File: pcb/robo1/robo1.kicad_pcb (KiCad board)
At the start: 2 copper layers, 9 parts, among them J1 Conn_02x05_Odd_Even, J2 Conn_02x05_Odd_Even, J3 Conn_01x05_Pin, J4 Conn_01x05_Pin, U1 Pico

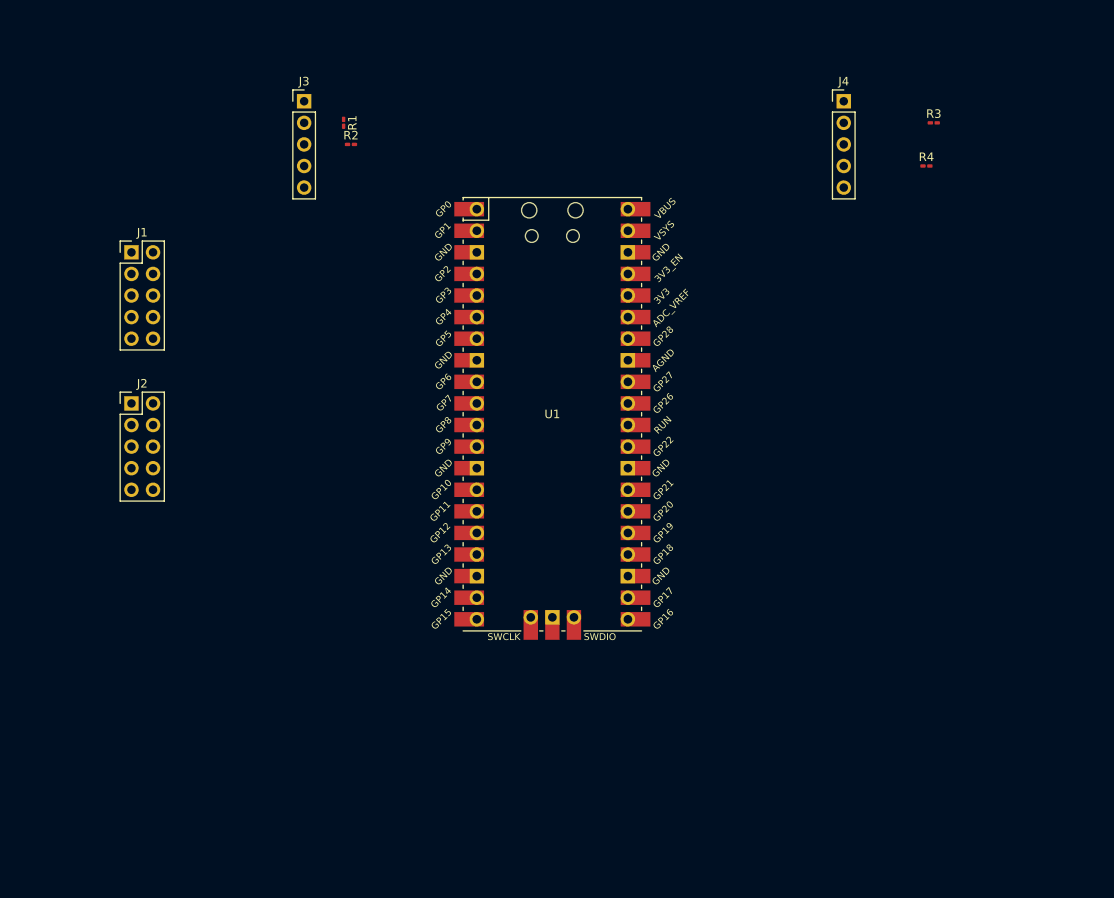
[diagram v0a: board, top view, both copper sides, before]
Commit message: pcb  outline
added mounting holes and text labels
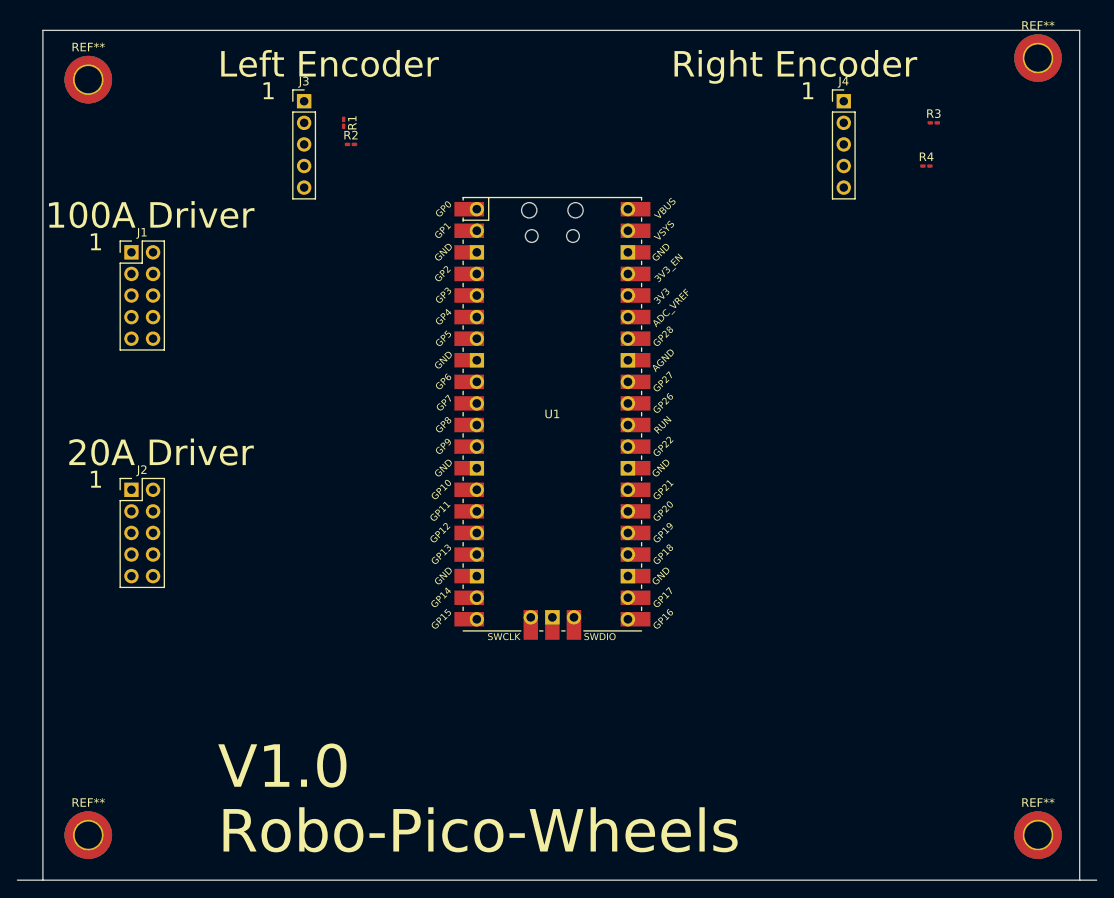
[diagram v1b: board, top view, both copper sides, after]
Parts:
- added REF**: MountingHole_3.2mm_M3_DIN965_Pad_TopBottom, MountingHole:MountingHole_3.2mm_M3_DIN965_Pad_TopBottom, F.Cu at (165.1, 48.3)
- added REF**: MountingHole_3.2mm_M3_DIN965_Pad_TopBottom, MountingHole:MountingHole_3.2mm_M3_DIN965_Pad_TopBottom, F.Cu at (53.3, 50.8)
- added REF**: MountingHole_3.2mm_M3_DIN965_Pad_TopBottom, MountingHole:MountingHole_3.2mm_M3_DIN965_Pad_TopBottom, F.Cu at (165.1, 139.7)
- added REF**: MountingHole_3.2mm_M3_DIN965_Pad_TopBottom, MountingHole:MountingHole_3.2mm_M3_DIN965_Pad_TopBottom, F.Cu at (53.3, 139.7)
- moved J2 10.2 mm to (58.4, 99.1)
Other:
- board outline added: 127 x 100 mm
- board text added: "1"
- board text added: "100A Driver"
- board text added: "20A Driver"
- board text added: "Left Encoder"
- board text added: "Right Encoder"
- board text added: "Robo-Pico-Wheels"
- board text added: "V1.0"
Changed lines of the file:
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@@
   )
   (setup
+    (stackup
+      (layer "F.SilkS" (type "Top Silk Screen"))
+      (layer "F.Paste" (type "Top Solder Paste"))
+      (layer "F.Mask" (type "Top Solder Mask") (thickness 0.01))
+      (layer "F.Cu" (type "copper") (thickness 0.035))
+      (layer "dielectric 1" (type "core") (thickness 1.51) (material "FR4") (epsilon_r 4.5) (loss_tangent 0.02))
+      (layer "B.Cu" (type "copper") (thickness 0.035))
+      (layer "B.Mask" (type "Bottom Solder Mask") (thickness 0.01))
+      (layer "B.Paste" (type "Bottom Solder Paste"))
+      (layer "B.SilkS" (type "Bottom Silk Screen"))
+      (copper_finish "ENIG")
+      (dielectric_constraints no)
+    )
     (pad_to_mask_clearance 0)
     (pcbplotparams
@@
   (net 39 "unconnected-(U1-SWCLK-Pad41)")
   (net 40 "unconnected-(U1-SWDIO-Pad43)")
+  (footprint "MountingHole:MountingHole_3.2mm_M3_DIN965_Pad_TopBottom" (layer "F.Cu")
+    (at 165.1 48.26)
+    (descr "Mounting Hole 3.2mm, M3, DIN965")
+    (tags "mounting hole 3.2mm m3 din965")
+    (attr exclude_from_pos_files exclude_from_bom)
+    (fp_text reference "REF**" (at 0 -3.8) (layer "F.SilkS")
+        (effects (font (size 1 1) (thickness 0.15)))
+    )
+    (fp_text value "MountingHole_3.2mm_M3_DIN965_Pad_TopBottom" (at 0 3.8) (layer "F.Fab")
+        (effects (font (size 1 1) (thickness 0.15)))
+    )
+    (fp_text user "${REFERENCE}" (at 0 0) (layer "F.Fab")
+        (effects (font (size 1 1) (thickness 0.15)))
+    )
+    (fp_circle (center 0 0) (end 2.8 0)
+      (stroke (width 0.15) (type solid)) (fill none) (layer "Cmts.User"))
+    (fp_circle (center 0 0) (end 3.05 0)
+      (stroke (width 0.05) (type solid)) (fill none) (layer "F.CrtYd"))
+    (pad "1" thru_hole circle (at 0 0) (size 3.6 3.6) (drill 3.2) (layers "*.Cu" "*.Mask"))
+    (pad "1" connect circle (at 0 0) (size 5.6 5.6) (layers "F.Cu" "F.Mask"))
+    (pad "1" connect circle (at 0 0) (size 5.6 5.6) (layers "B.Cu" "B.Mask"))
+  )
   (footprint "Resistor_SMD:R_0201_0603Metric_Pad0.64x0.40mm_HandSolder" (layer "F.Cu")
     (at 83.3875 55.88 -90)
@@
     )
   )
+  (footprint "MountingHole:MountingHole_3.2mm_M3_DIN965_Pad_TopBottom" (layer "F.Cu")
+    (at 53.34 50.8)
+    (descr "Mounting Hole 3.2mm, M3, DIN965")
+    (tags "mounting hole 3.2mm m3 din965")
+    (attr exclude_from_pos_files exclude_from_bom)
+    (fp_text reference "REF**" (at 0 -3.8) (layer "F.SilkS")
+        (effects (font (size 1 1) (thickness 0.15)))
+    )
+    (fp_text value "MountingHole_3.2mm_M3_DIN965_Pad_TopBottom" (at 0 3.8) (layer "F.Fab")
+        (effects (font (size 1 1) (thickness 0.15)))
+    )
+    (fp_text user "${REFERENCE}" (at 0 0) (layer "F.Fab")
+        (effects (font (size 1 1) (thickness 0.15)))
+    )
+    (fp_circle (center 0 0) (end 2.8 0)
+      (stroke (width 0.15) (type solid)) (fill none) (layer "Cmts.User"))
+    (fp_circle (center 0 0) (end 3.05 0)
+      (stroke (width 0.05) (type solid)) (fill none) (layer "F.CrtYd"))
+    (pad "1" thru_hole circle (at 0 0) (size 3.6 3.6) (drill 3.2) (layers "*.Cu" "*.Mask"))
+    (pad "1" connect circle (at 0 0) (size 5.6 5.6) (layers "F.Cu" "F.Mask"))
+    (pad "1" connect circle (at 0 0) (size 5.6 5.6) (layers "B.Cu" "B.Mask"))
+  )
   (footprint "Connector_PinHeader_2.54mm:PinHeader_2x05_P2.54mm_Vertical" (layer "F.Cu")
-    (at 58.42 88.9)
+    (at 58.42 99.06)
     (descr "Through hole straight pin header, 2x05, 2.54mm pitch, double rows")
     (tags "Through hole pin header THT 2x05 2.54mm double row")
@@
     )
   )
+  (footprint "MountingHole:MountingHole_3.2mm_M3_DIN965_Pad_TopBottom" (layer "F.Cu")
+    (at 165.1 139.7)
+    (descr "Mounting Hole 3.2mm, M3, DIN965")
+    (tags "mounting hole 3.2mm m3 din965")
+    (attr exclude_from_pos_files exclude_from_bom)
+    (fp_text reference "REF**" (at 0 -3.8) (layer "F.SilkS")
+        (effects (font (size 1 1) (thickness 0.15)))
+    )
+    (fp_text value "MountingHole_3.2mm_M3_DIN965_Pad_TopBottom" (at 0 3.8) (layer "F.Fab")
+        (effects (font (size 1 1) (thickness 0.15)))
+    )
+    (fp_text user "${REFERENCE}" (at 0 0) (layer "F.Fab")
+        (effects (font (size 1 1) (thickness 0.15)))
+    )
+    (fp_circle (center 0 0) (end 2.8 0)
+      (stroke (width 0.15) (type solid)) (fill none) (layer "Cmts.User"))
+    (fp_circle (center 0 0) (end 3.05 0)
+      (stroke (width 0.05) (type solid)) (fill none) (layer "F.CrtYd"))
+    (pad "1" thru_hole circle (at 0 0) (size 3.6 3.6) (drill 3.2) (layers "*.Cu" "*.Mask"))
+    (pad "1" connect circle (at 0 0) (size 5.6 5.6) (layers "F.Cu" "F.Mask"))
+    (pad "1" connect circle (at 0 0) (size 5.6 5.6) (layers "B.Cu" "B.Mask"))
+  )
   (footprint "Resistor_SMD:R_0201_0603Metric_Pad0.64x0.40mm_HandSolder" (layer "F.Cu")
     (at 84.2525 58.42)
@@
       (rotate (xyz 0 0 0))
     )
+  )
+  (footprint "MountingHole:MountingHole_3.2mm_M3_DIN965_Pad_TopBottom" (layer "F.Cu")
+    (at 53.34 139.7)
+    (descr "Mounting Hole 3.2mm, M3, DIN965")
+    (tags "mounting hole 3.2mm m3 din965")
+    (attr exclude_from_pos_files exclude_from_bom)
+    (fp_text reference "REF**" (at 0 -3.8) (layer "F.SilkS")
+        (effects (font (size 1 1) (thickness 0.15)))
+    )
+    (fp_text value "MountingHole_3.2mm_M3_DIN965_Pad_TopBottom" (at 0 3.8) (layer "F.Fab")
+        (effects (font (size 1 1) (thickness 0.15)))
+    )
+    (fp_text user "${REFERENCE}" (at 0 0) (layer "F.Fab")
+        (effects (font (size 1 1) (thickness 0.15)))
+    )
+    (fp_circle (center 0 0) (end 2.8 0)
+      (stroke (width 0.15) (type solid)) (fill none) (layer "Cmts.User"))
+    (fp_circle (center 0 0) (end 3.05 0)
+      (stroke (width 0.05) (type solid)) (fill none) (layer "F.CrtYd"))
+    (pad "1" thru_hole circle (at 0 0) (size 3.6 3.6) (drill 3.2) (layers "*.Cu" "*.Mask"))
+    (pad "1" connect circle (at 0 0) (size 5.6 5.6) (layers "F.Cu" "F.Mask"))
+    (pad "1" connect circle (at 0 0) (size 5.6 5.6) (layers "B.Cu" "B.Mask"))
   )
   (footprint "Resistor_SMD:R_0201_0603Metric_Pad0.64x0.40mm_HandSolder" (layer "F.Cu")
@@
     )
   )
+  (gr_line (start 172 145) (end 45 145)
+    (stroke (width 0.1) (type default)) (layer "Edge.Cuts"))
+  (gr_line (start 170 45) (end 170 145)
+    (stroke (width 0.1) (type default)) (layer "Edge.Cuts"))
+  (gr_line (start 48 145) (end 48 45)
+    (stroke (width 0.1) (type default)) (layer "Edge.Cuts"))
+  (gr_line (start 48 45) (end 170 45)
+    (stroke (width 0.1) (type default)) (layer "Edge.Cuts"))
+  (gr_text "V1.0" (at 68.58 134.62) (layer "F.SilkS")
+    (effects (font (size 5 5) (thickness 0.2)) (justify left bottom))
+  )
+  (gr_text "Robo-Pico-Wheels" (at 68.58 142.24) (layer "F.SilkS")
+    (effects (font (size 5 5) (thickness 0.2)) (justify left bottom))
+  )
+  (gr_text "100A Driver" (at 48.26 68.58) (layer "F.SilkS")
+    (effects (font (size 3 3) (thickness 0.2)) (justify left bottom))
+  )
+  (gr_text "1" (at 73.66 53.34) (layer "F.SilkS")
+    (effects (font (size 2 2) (thickness 0.15)) (justify left bottom))
+  )
+  (gr_text "1" (at 53.34 99.06) (layer "F.SilkS")
+    (effects (font (size 2 2) (thickness 0.15)) (justify left bottom))
+  )
+  (gr_text "1" (at 53.34 71.12) (layer "F.SilkS")
+    (effects (font (size 2 2) (thickness 0.15)) (justify left bottom))
+  )
+  (gr_text "Left Encoder" (at 68.58 50.8) (layer "F.SilkS")
+    (effects (font (size 3 3) (thickness 0.2)) (justify left bottom))
+  )
+  (gr_text "20A Driver" (at 50.8 96.52) (layer "F.SilkS")
+    (effects (font (size 3 3) (thickness 0.2)) (justify left bottom))
+  )
+  (gr_text "Right Encoder" (at 121.92 50.8) (layer "F.SilkS")
+    (effects (font (size 3 3) (thickness 0.2)) (justify left bottom))
+  )
+  (gr_text "1" (at 137.16 53.34) (layer "F.SilkS")
+    (effects (font (size 2 2) (thickness 0.15)) (justify left bottom))
+  )
 )

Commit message: Add OLED to PCB
OLED added to pcb
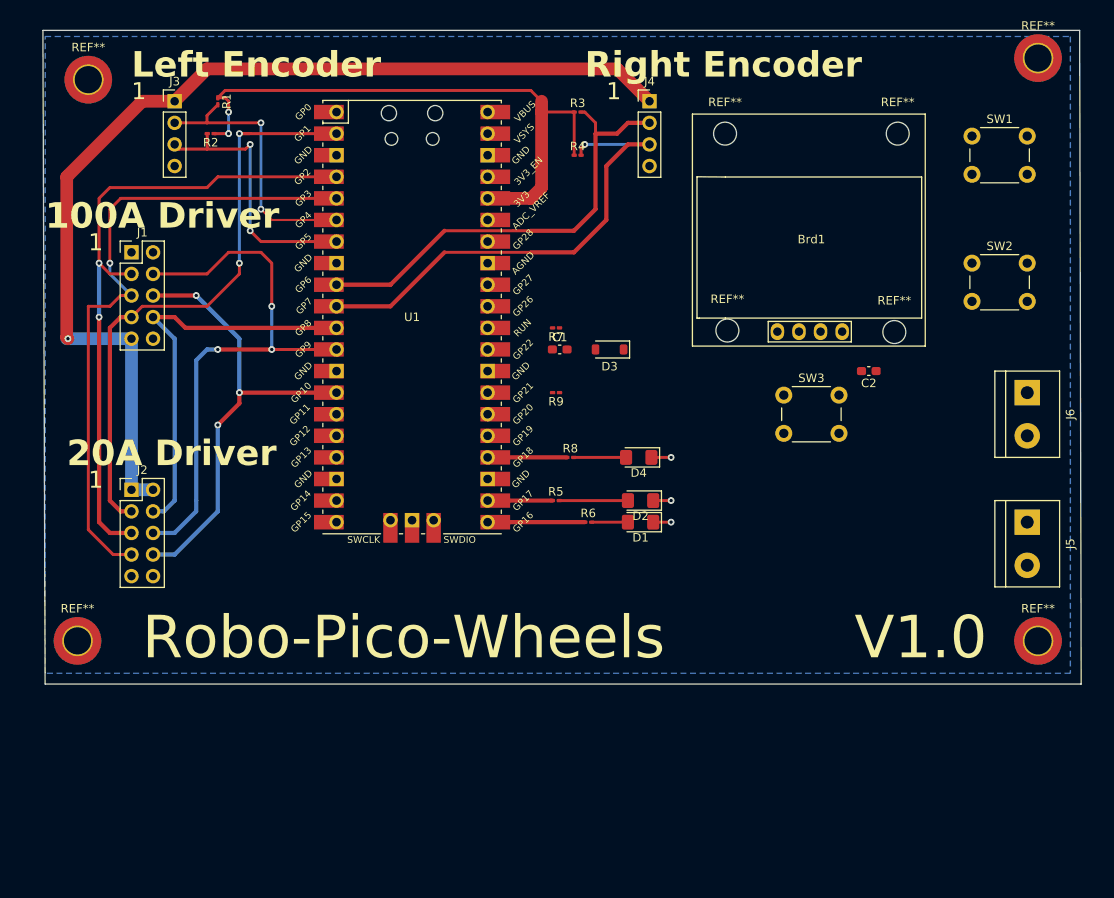
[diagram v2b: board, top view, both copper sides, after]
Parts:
- added Brd1: SSD1306, SSD1306:128x64OLED, F.Cu at (138.4, 69.8)
- added C1: .01, Capacitor_SMD:C_0603_1608Metric_Pad1.08x0.95mm_HandSolder, F.Cu at (108.8, 82.5)
- added C2: .01, Capacitor_SMD:C_0603_1608Metric_Pad1.08x0.95mm_HandSolder, F.Cu at (145.2, 85.1)
- added D1: LED, LED_SMD:LED_1206_3216Metric_Pad1.42x1.75mm_HandSolder, F.Cu at (118.3, 102.9)
- added D2: LED, LED_SMD:LED_1206_3216Metric_Pad1.42x1.75mm_HandSolder, F.Cu at (118.3, 100.3)
- added D3: 1N4148W, Diode_SMD:D_SOD-123, F.Cu at (114.7, 82.5)
- added D4: LED, LED_SMD:LED_1206_3216Metric_Pad1.42x1.75mm_HandSolder, F.Cu at (118.1, 95.2)
- added J5: Screw_Terminal_01x02, TerminalBlock:TerminalBlock_bornier-2_P5.08mm, F.Cu at (163.8, 102.9)
- added J6: Screw_Terminal_01x02, TerminalBlock:TerminalBlock_bornier-2_P5.08mm, F.Cu at (163.8, 87.6)
- added R5: 220, Resistor_SMD:R_0201_0603Metric_Pad0.64x0.40mm_HandSolder, F.Cu at (108.4, 100.3)
- added R6: 220, Resistor_SMD:R_0201_0603Metric_Pad0.64x0.40mm_HandSolder, F.Cu at (112.2, 102.9)
- added R7: 4.7K, Resistor_SMD:R_0201_0603Metric_Pad0.64x0.40mm_HandSolder, F.Cu at (108.4, 80.0)
- added R8: 220, Resistor_SMD:R_0201_0603Metric_Pad0.64x0.40mm_HandSolder, F.Cu at (110.1, 95.2)
- added R9: 4.7K, Resistor_SMD:R_0201_0603Metric_Pad0.64x0.40mm_HandSolder, F.Cu at (108.4, 87.6)
- added REF**: MountingHole_2.7mm_M2.5, MountingHole:MountingHole_2.7mm_M2.5, F.Cu at (148.6, 57.1)
- added REF**: MountingHole_2.7mm_M2.5, MountingHole:MountingHole_2.7mm_M2.5, F.Cu at (148.2, 80.5)
- added REF**: MountingHole_2.7mm_M2.5, MountingHole:MountingHole_2.7mm_M2.5, F.Cu at (128.3, 57.1)
- added REF**: MountingHole_2.7mm_M2.5, MountingHole:MountingHole_2.7mm_M2.5, F.Cu at (128.5, 80.3)
- added SW1: SW_Push, Button_Switch_THT:SW_PUSH_6mm, F.Cu at (157.3, 57.4)
- added SW2: SW_Push, Button_Switch_THT:SW_PUSH_6mm, F.Cu at (157.3, 72.4)
- added SW3: SW_Push, Button_Switch_THT:SW_PUSH_6mm, F.Cu at (135.2, 87.9)
- J3, J4: value Conn_01x05_Pin -> Conn_01x04_Pin; footprint Connector_PinHeader_2.54mm:PinHeader_1x05_P2.54mm_Vertical -> Connector_PinHeader_2.54mm:PinHeader_1x04_P2.54mm_Vertical
- moved R3 41.9 mm to (110.9, 54.6)
- moved R4 41.1 mm to (110.9, 59.7)
- moved REF** 22.9 mm to (52.1, 116.8)
- moved J4 22.9 mm to (119.4, 53.3)
- moved REF** 22.9 mm to (165.1, 116.8)
- moved U1 20.1 mm to (91.4, 78.7)
- moved R2 16.6 mm to (67.7, 57.1), turned to 180 degrees
- moved J3 15.2 mm to (63.5, 53.3)
- moved R1 15.0 mm to (68.6, 53.3)
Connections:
- U1 pad 15: unconnected-(U1-GPIO11-Pad15) -> /PWM_LEFT
- U1 pad 2: /PWM_LEFT -> unconnected-(U1-GPIO1-Pad2)
- U1 pad 21: unconnected-(U1-GPIO16-Pad21) -> Net-(U1-GPIO16)
- U1 pad 22: unconnected-(U1-GPIO17-Pad22) -> Net-(U1-GPIO17)
- U1 pad 24: unconnected-(U1-GPIO18-Pad24) -> Net-(U1-GPIO18)
- U1 pad 25: unconnected-(U1-GPIO19-Pad25) -> /I2C1_SCL
- U1 pad 26: unconnected-(U1-GPIO20-Pad26) -> /I2C1_SDA
- U1 pad 29: unconnected-(U1-GPIO22-Pad29) -> Net-(D3-A)
- U1 pad 36: unconnected-(U1-3V3-Pad36) -> +3.3V
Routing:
- net +5V: track 0.00 -> 122.5 mm, vias 0 -> 1
- net /LEFTDIRB: track 0.00 -> 76.6 mm, vias 0 -> 1
- net /LEFTDIRA: track 0.00 -> 75.8 mm, vias 0 -> 2
- net +3.3V: track 0.00 -> 71.9 mm, vias 0 -> 2
- net /PWM_LEFT: track 0.00 -> 70.5 mm, vias 0 -> 2
- net /RIGHTDIRA: track 0.00 -> 66.7 mm, vias 0 -> 3
- net /RIGHTENCB: track 0.00 -> 57.5 mm, vias 0 -> 1
- net /RIGHTDIRB: track 0.00 -> 54.8 mm, vias 0 -> 3
- net /RIGHTENCA: track 0.00 -> 53.4 mm
- net /PWM_RIGHT: track 0.00 -> 47.8 mm
- net /LEFTENCA: track 0.00 -> 32.4 mm, vias 0 -> 2
- net /LEFTENCB: track 0.00 -> 32.0 mm, vias 0 -> 2
- net Net-(U1-GPIO16): track 0.00 -> 11.4 mm
- net Net-(U1-GPIO18): track 0.00 -> 9.32 mm
- net Net-(D2-A): track 0.00 -> 8.08 mm
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- added copper zone on B.Cu, net GND
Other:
- board size 127 x 100 mm -> 122.2 x 76.9 mm
